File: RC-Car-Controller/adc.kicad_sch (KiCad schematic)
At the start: 4 parts, among them U3 ADC082S021CIMM/NOPB

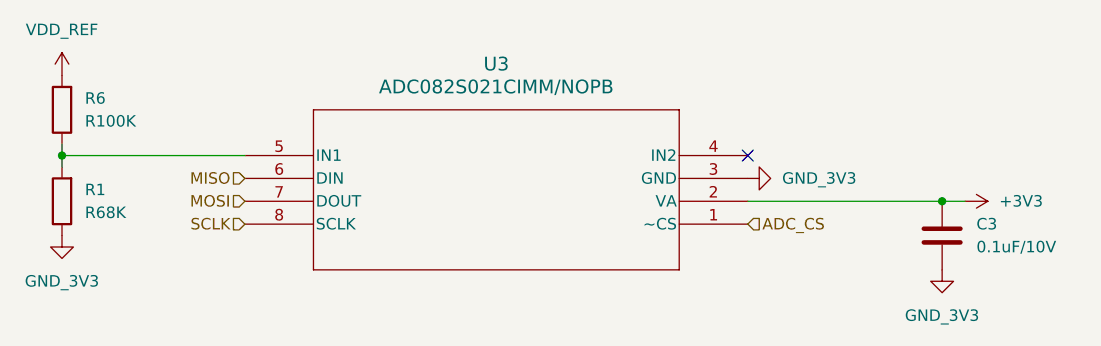
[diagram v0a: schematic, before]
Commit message: Added Camera Connector, Minor Controller Fixes
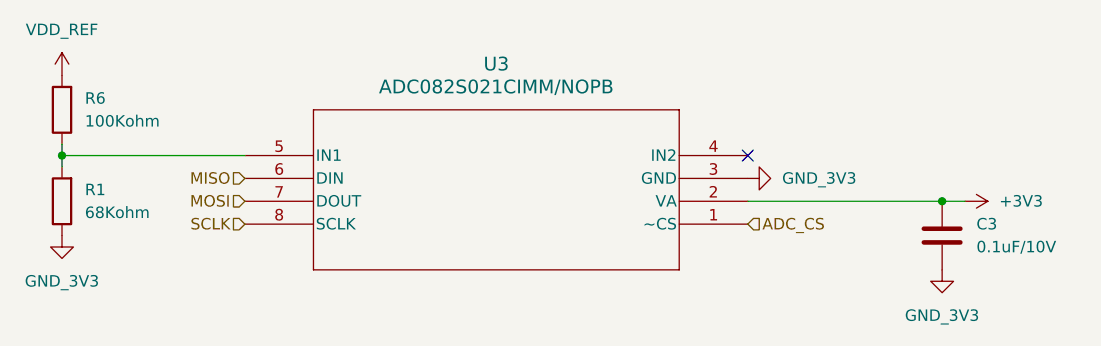
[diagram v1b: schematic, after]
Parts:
- R1: value R68K -> 68Kohm
- R6: value R100K -> 100Kohm
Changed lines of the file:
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@@
 			)
 		)
-		(property "Value" "R68K"
+		(property "Value" "68Kohm"
 			(at 88.9 96.5199 0)
 			(effects
@@
 			)
 		)
-		(property "Value" "R100K"
+		(property "Value" "100Kohm"
 			(at 88.9 86.3599 0)
 			(effects
